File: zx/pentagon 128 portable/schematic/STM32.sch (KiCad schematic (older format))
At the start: 15 parts

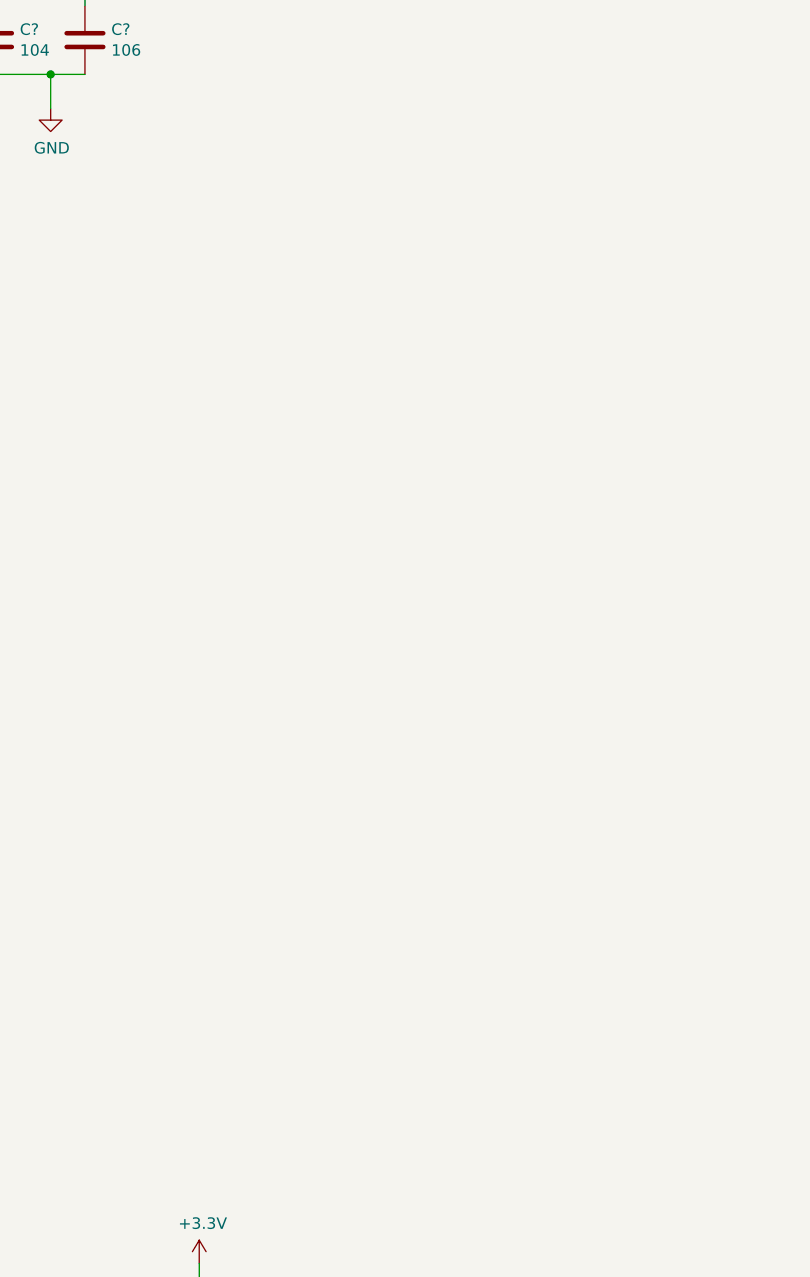
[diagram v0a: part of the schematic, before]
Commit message: added memory devboard, moved devboard to schematic
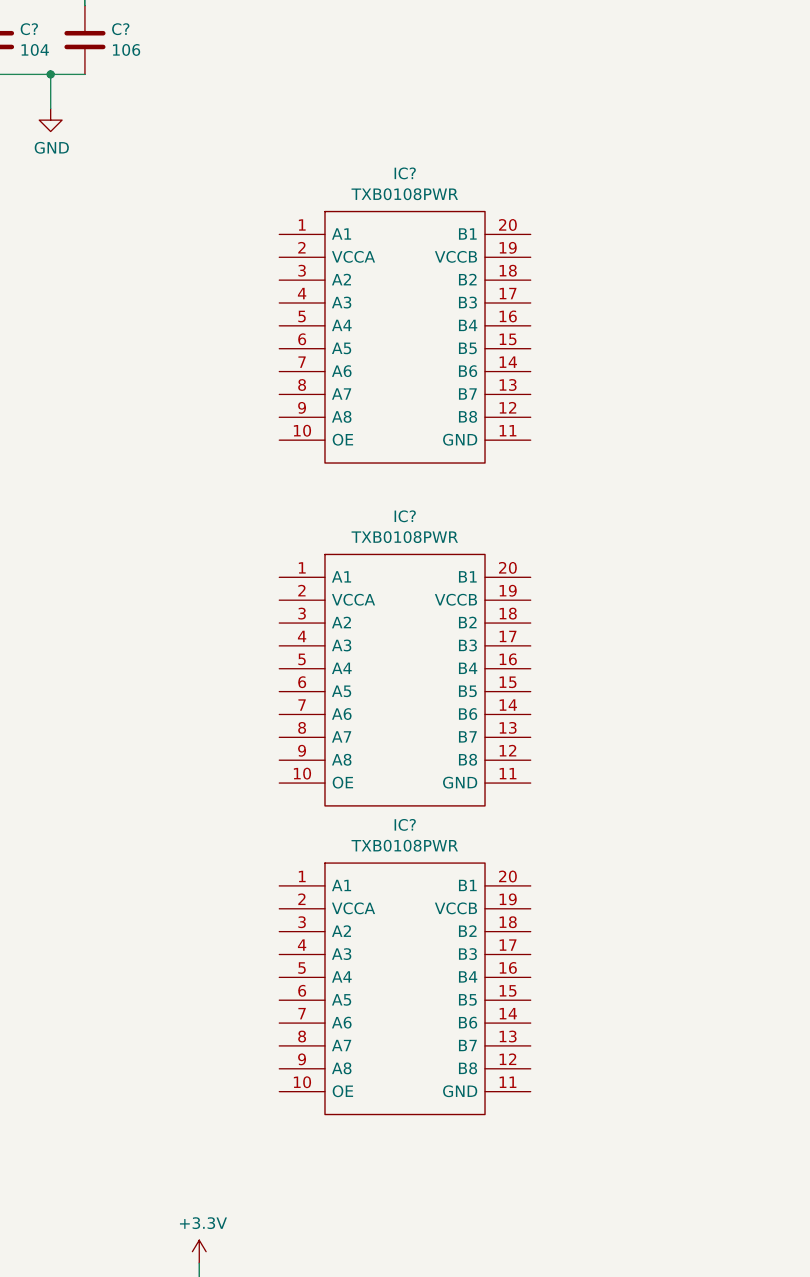
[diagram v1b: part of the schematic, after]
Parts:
- added IC? (x3): TXB0108PWR, SOP65P640X120-20N, symbol SamacSys_Parts:TXB0108PWR
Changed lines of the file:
@@
+	1    0    0    -1
+$EndComp
+$Comp
+L SamacSys_Parts:TXB0108PWR IC?
+U 1 1 5F5F8283
+P 6700 1850
+F 0 "IC?" H 7250 2115 50  0000 C CNN
+F 1 "TXB0108PWR" H 7250 2024 50  0000 C CNN
+F 2 "SOP65P640X120-20N" H 7650 1950 50  0001 L CNN
+F 3 "http://www.ti.com/lit/ds/symlink/txb0108.pdf" H 7650 1850 50  0001 L CNN
+F 4 "8-Bit Bidirectional Voltage-Level Shifter with Auto Direction Sensing and +/-15-kV ESD Protect" H 7650 1750 50  0001 L CNN "Description"
+F 5 "1.2" H 7650 1650 50  0001 L CNN "Height"
+F 6 "595-TXB0108PWR" H 7650 1550 50  0001 L CNN "Mouser Part Number"
+F 7 "https://www.mouser.co.uk/ProductDetail/Texas-Instruments/TXB0108PWR?qs=oFXvjAmG9EgEUWGWzOVFCA%3D%3D" H 7650 1450 50  0001 L CNN "Mouser Price/Stock"
+F 8 "Texas Instruments" H 7650 1350 50  0001 L CNN "Manufacturer_Name"
+F 9 "TXB0108PWR" H 7650 1250 50  0001 L CNN "Manufacturer_Part_Number"
+	1    6700 1850
+	1    0    0    -1
+$EndComp
+$Comp
+L SamacSys_Parts:TXB0108PWR IC?
+U 1 1 5F5F8E20
+P 6700 3350
+F 0 "IC?" H 7250 3615 50  0000 C CNN
+F 1 "TXB0108PWR" H 7250 3524 50  0000 C CNN
+F 2 "SOP65P640X120-20N" H 7650 3450 50  0001 L CNN
+F 3 "http://www.ti.com/lit/ds/symlink/txb0108.pdf" H 7650 3350 50  0001 L CNN
+F 4 "8-Bit Bidirectional Voltage-Level Shifter with Auto Direction Sensing and +/-15-kV ESD Protect" H 7650 3250 50  0001 L CNN "Description"
+F 5 "1.2" H 7650 3150 50  0001 L CNN "Height"
+F 6 "595-TXB0108PWR" H 7650 3050 50  0001 L CNN "Mouser Part Number"
+F 7 "https://www.mouser.co.uk/ProductDetail/Texas-Instruments/TXB0108PWR?qs=oFXvjAmG9EgEUWGWzOVFCA%3D%3D" H 7650 2950 50  0001 L CNN "Mouser Price/Stock"
+F 8 "Texas Instruments" H 7650 2850 50  0001 L CNN "Manufacturer_Name"
+F 9 "TXB0108PWR" H 7650 2750 50  0001 L CNN "Manufacturer_Part_Number"
+	1    6700 3350
+	1    0    0    -1
+$EndComp
+$Comp
+L SamacSys_Parts:TXB0108PWR IC?
+U 1 1 5F5F9A70
+P 6700 4700
+F 0 "IC?" H 7250 4965 50  0000 C CNN
+F 1 "TXB0108PWR" H 7250 4874 50  0000 C CNN
+F 2 "SOP65P640X120-20N" H 7650 4800 50  0001 L CNN
+F 3 "http://www.ti.com/lit/ds/symlink/txb0108.pdf" H 7650 4700 50  0001 L CNN
+F 4 "8-Bit Bidirectional Voltage-Level Shifter with Auto Direction Sensing and +/-15-kV ESD Protect" H 7650 4600 50  0001 L CNN "Description"
+F 5 "1.2" H 7650 4500 50  0001 L CNN "Height"
+F 6 "595-TXB0108PWR" H 7650 4400 50  0001 L CNN "Mouser Part Number"
+F 7 "https://www.mouser.co.uk/ProductDetail/Texas-Instruments/TXB0108PWR?qs=oFXvjAmG9EgEUWGWzOVFCA%3D%3D" H 7650 4300 50  0001 L CNN "Mouser Price/Stock"
+F 8 "Texas Instruments" H 7650 4200 50  0001 L CNN "Manufacturer_Name"
+F 9 "TXB0108PWR" H 7650 4100 50  0001 L CNN "Manufacturer_Part_Number"
+	1    6700 4700
 	1    0    0    -1
 $EndComp
